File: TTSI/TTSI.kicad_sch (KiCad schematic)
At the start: 36 parts, among them Q101 NMOS, Q102 NMOS, Q103 NMOS, Q104 PMOS, Q105 NMOS, Q106 NMOS, U101 641964-1, U102 641964-1, U103 R-78E5.0-0.5, U104 74AHC1G32, U105 641964-1, U106 74AHC1G08, U107 LM555xM

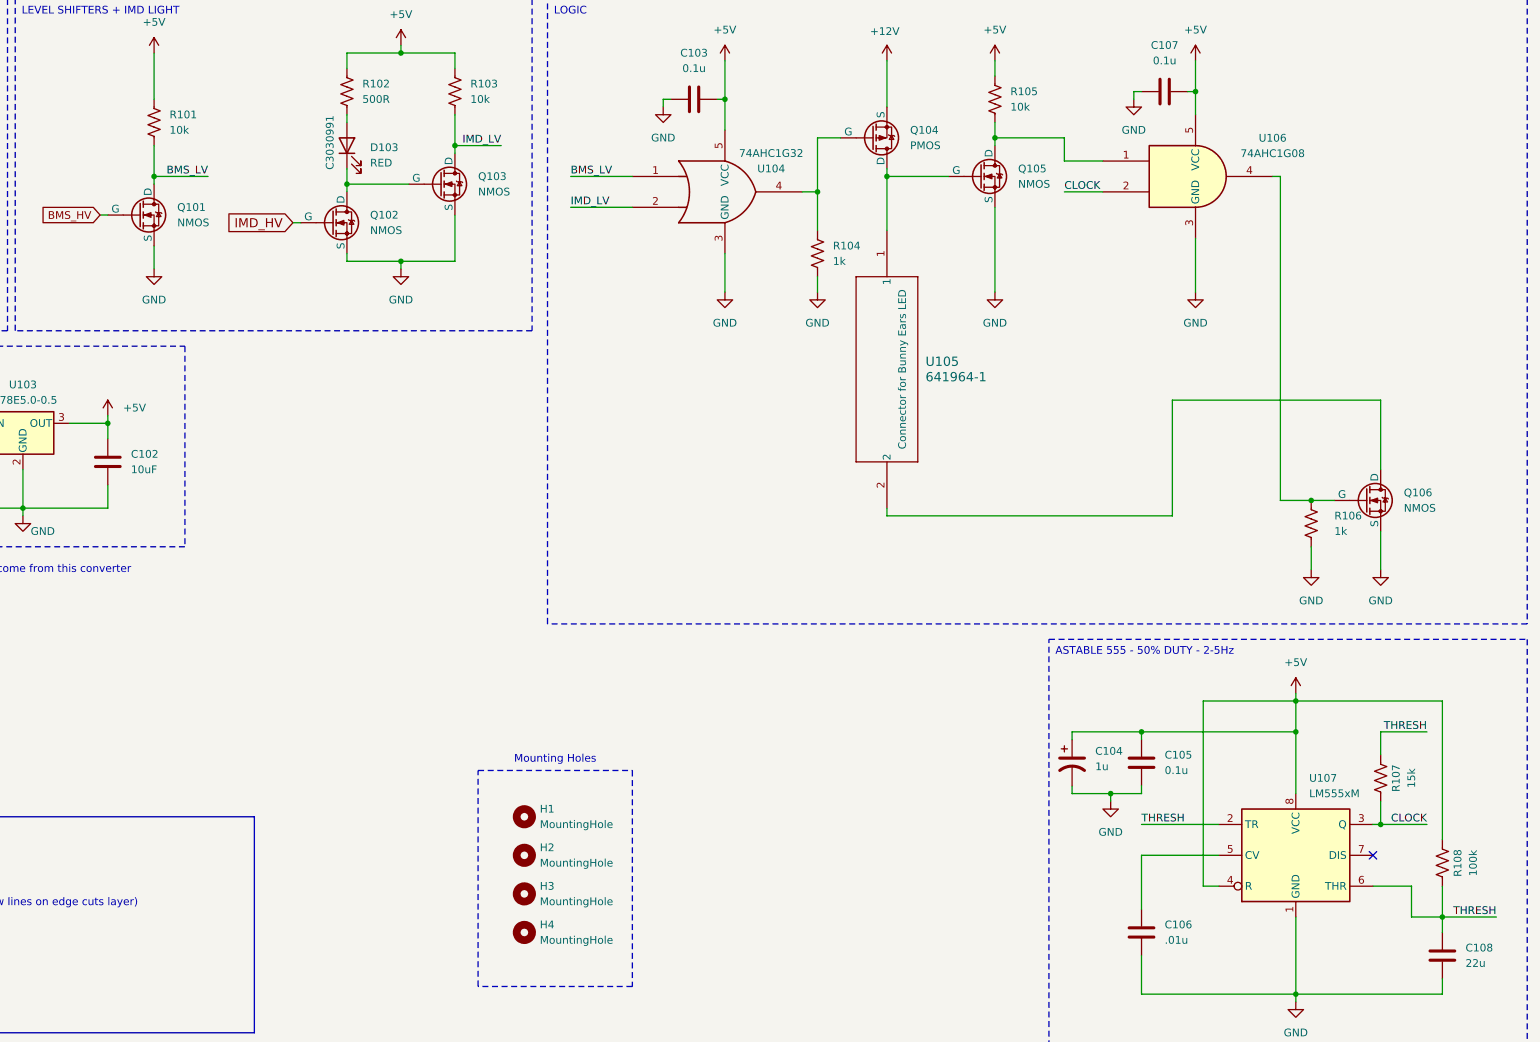
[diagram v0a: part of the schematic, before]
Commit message: Fixed TSSI footprint issues
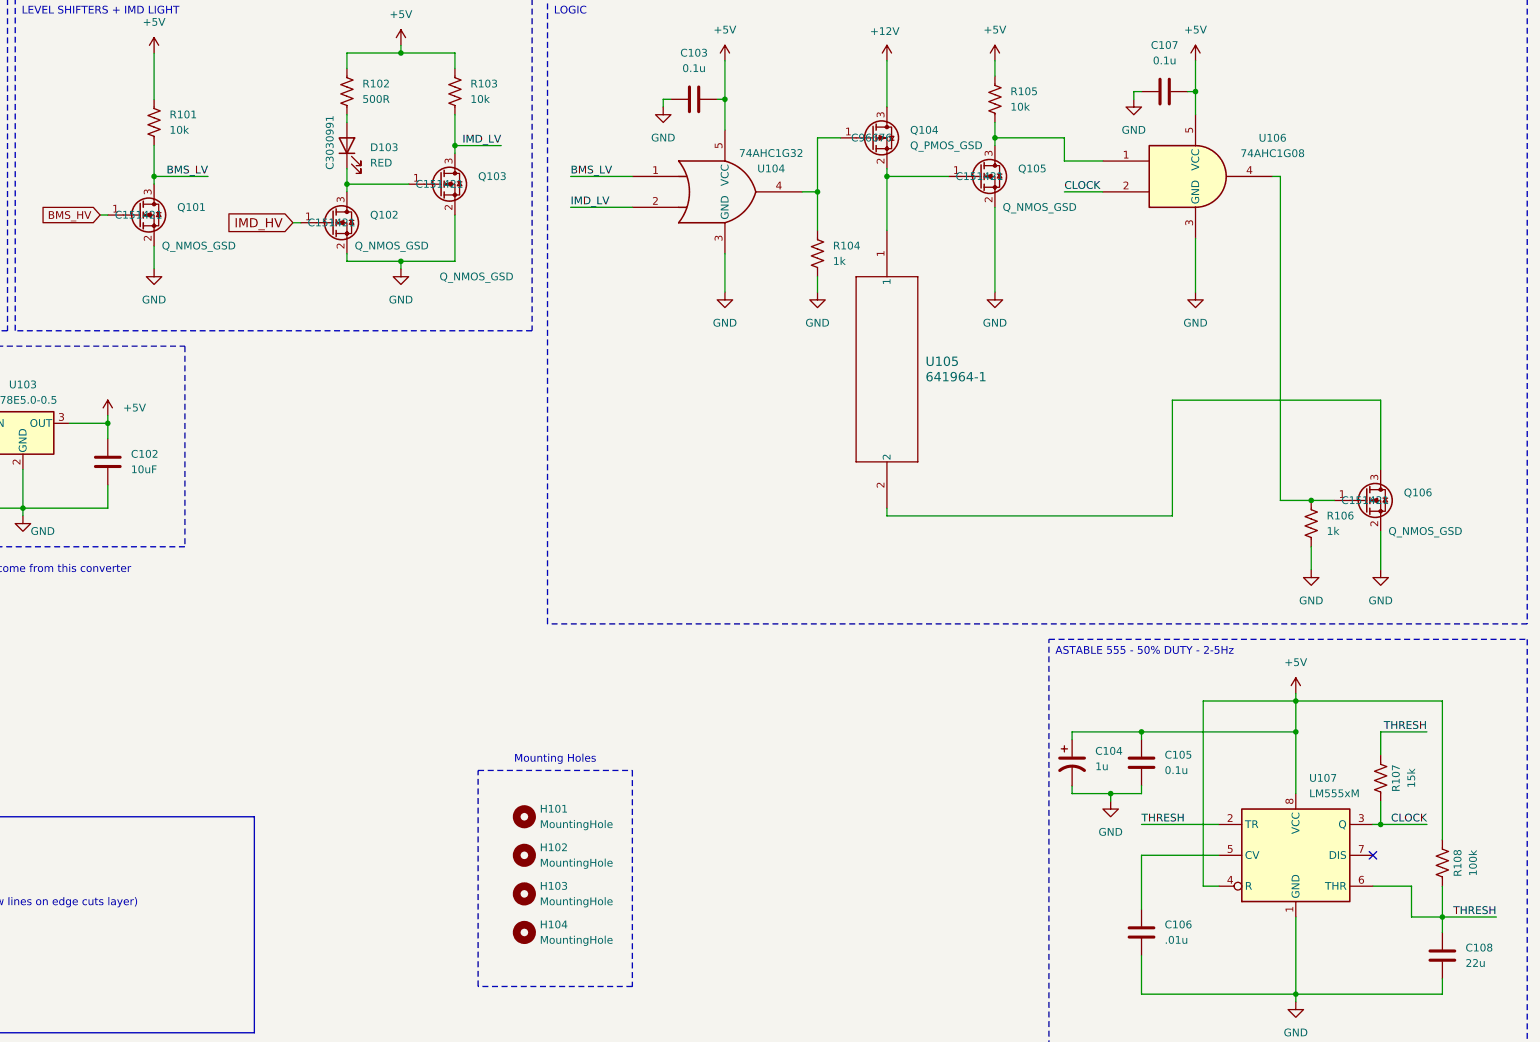
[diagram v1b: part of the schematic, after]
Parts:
- removed Q101, Q102, Q103, Q105, Q106: NMOS, Package_TO_SOT_SMD:SOT-23, symbol Simulation_SPICE:NMOS
- removed Q104: PMOS, Package_TO_SOT_SMD:SOT-523, symbol Simulation_SPICE:PMOS
- removed U101, U102: 641964-1, 641964-1:641964-1_TYC, symbol 641964-1:641964-1
- added Q101, Q102, Q103, Q105, Q106: Q_NMOS_GSD, Package_TO_SOT_SMD:SOT-23, symbol Transistor_FET:Q_NMOS_GSD
- added Q104: Q_PMOS_GSD, Package_TO_SOT_SMD:SOT-523, symbol Transistor_FET:Q_PMOS_GSD
- added U101, U102: 641964-1, CONNECTOR:641964-1_TYC, symbol CONNECTOR:641964-1
- U105: footprint 641964-1:641964-1_TYC -> CONNECTOR:641964-1_TYC
- renumbered H1 to H101, H2 to H102, H3 to H103, H4 to H104
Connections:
- net +12V: now also Q104.3 (D), U102.1
- net BMS_HV: now also Q101.1 (G), U101.1
- net BMS_LV: now also Q101.3 (D)
- net GND: now also Q101.2 (S), Q102.2 (S), Q103.2 (S), Q105.2 (S), Q106.2 (S), U102.2
- net IMD_HV: now also Q102.1 (G), U101.2
- net IMD_LV: now also Q103.3 (D)
- net at R105.2, U106.1: now also Q105.3 (D)
- net at R106.1, U106.4: now also Q106.1 (G)
- net at D103.1 (K): now also Q102.3 (D), Q103.1 (G)
- net at R104.1, U104.4: now also Q104.1 (G)
- net at U105.1: now also Q104.2 (S), Q105.1 (G)
- net at U105.2: now also Q106.3 (D)

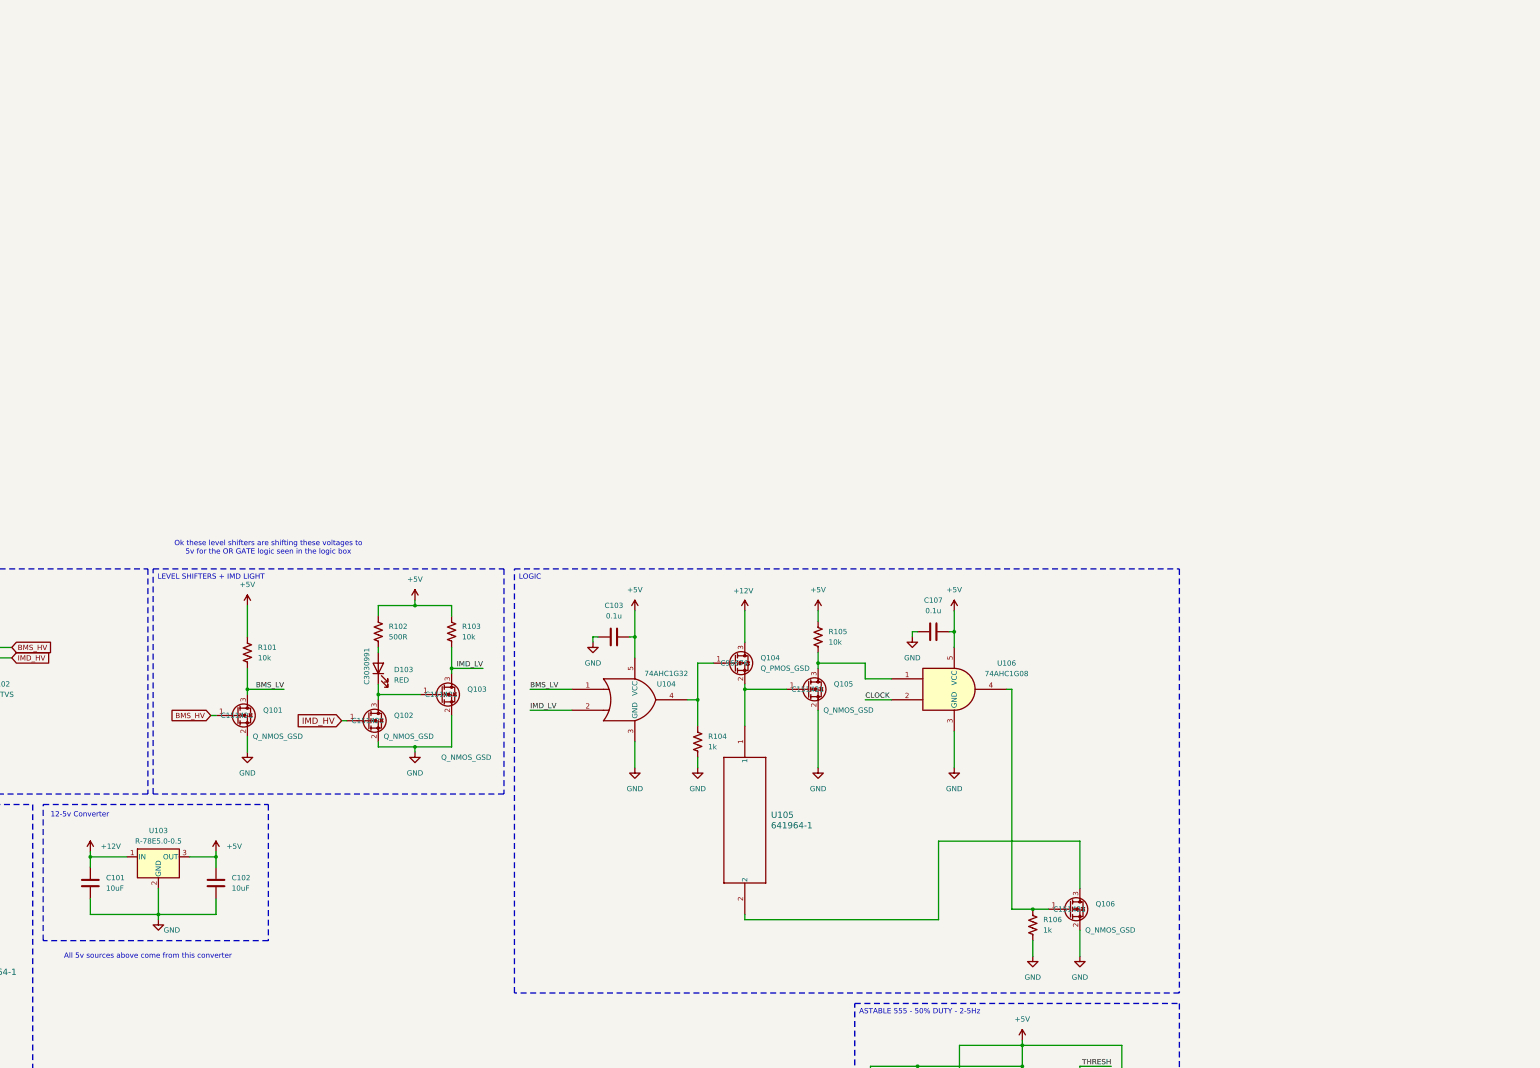
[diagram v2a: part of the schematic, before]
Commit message: TSSI has been integrated into fault latch.
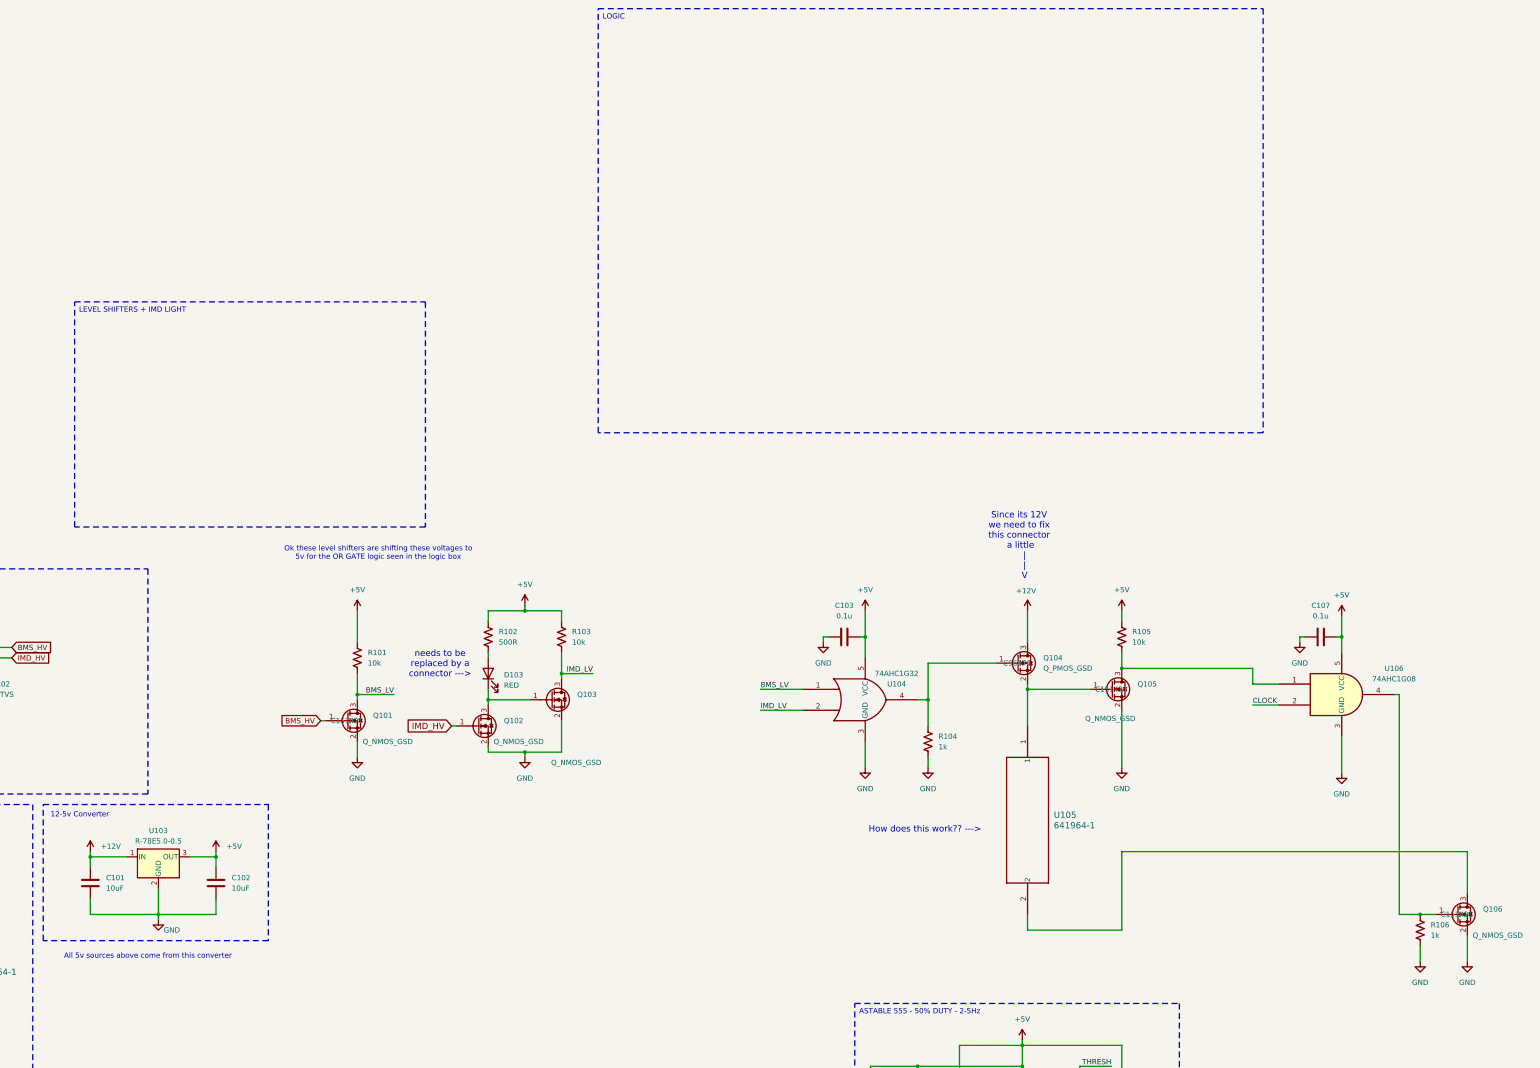
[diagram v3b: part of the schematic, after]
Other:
- note added: "How does this work?? --->"
- note added: "Since its 12V we need to fix this connector a little | | V"
- note added: "needs to be replaced by a connector --->"
- moved on the sheet: C103, C107, D103, Q101, Q102, Q103, Q104, Q105, Q106, R101, R102, R103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
